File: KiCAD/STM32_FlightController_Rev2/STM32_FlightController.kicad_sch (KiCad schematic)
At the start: 71 parts, among them J1 USB_B_Micro, J10 Serial Debug Pins, J11 GPS_V_{IN}, J12 GPS_TX, J13 GND, J14 GPS_RX, J15 ELRS_V_{IN}, J16 GND, J17 ELRS_TX, J18 ELRS_RX, J2 GND, J3 BAT, J4 CRT, J5 5V, J6 S1, J7 S2, J8 S3, J9 S4, Q1 IRLML6244, Q2 IRLML6244, SW1 PTS815SJM, SW2 SW_SPDT, U1 USBLC6-2SC6, U2 AMS1117-3.3, U3 TLV70018, U4 STM32F405RGTx, U5 BMP390L, U6 ICM-20948, Y1 8MHz

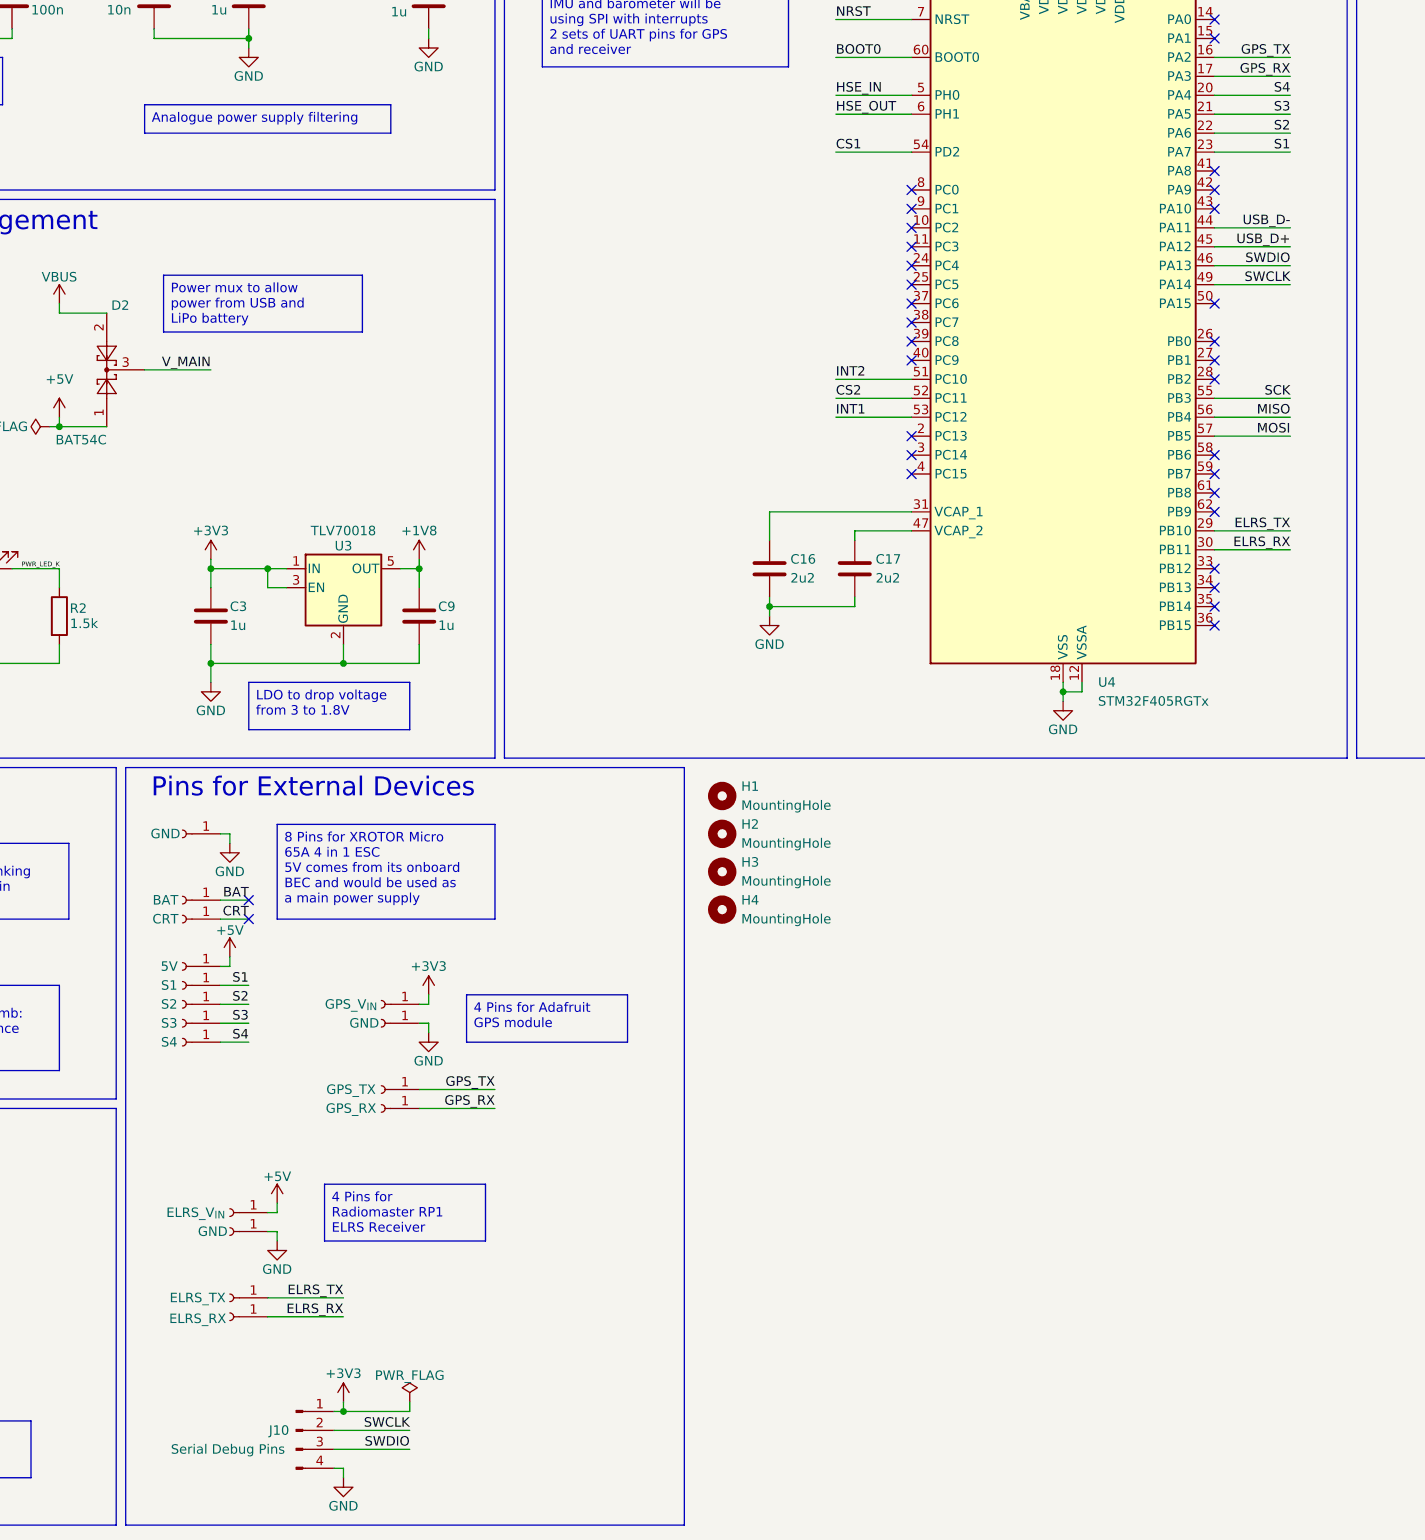
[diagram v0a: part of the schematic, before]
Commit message: added firmware framework, some PCB modifications
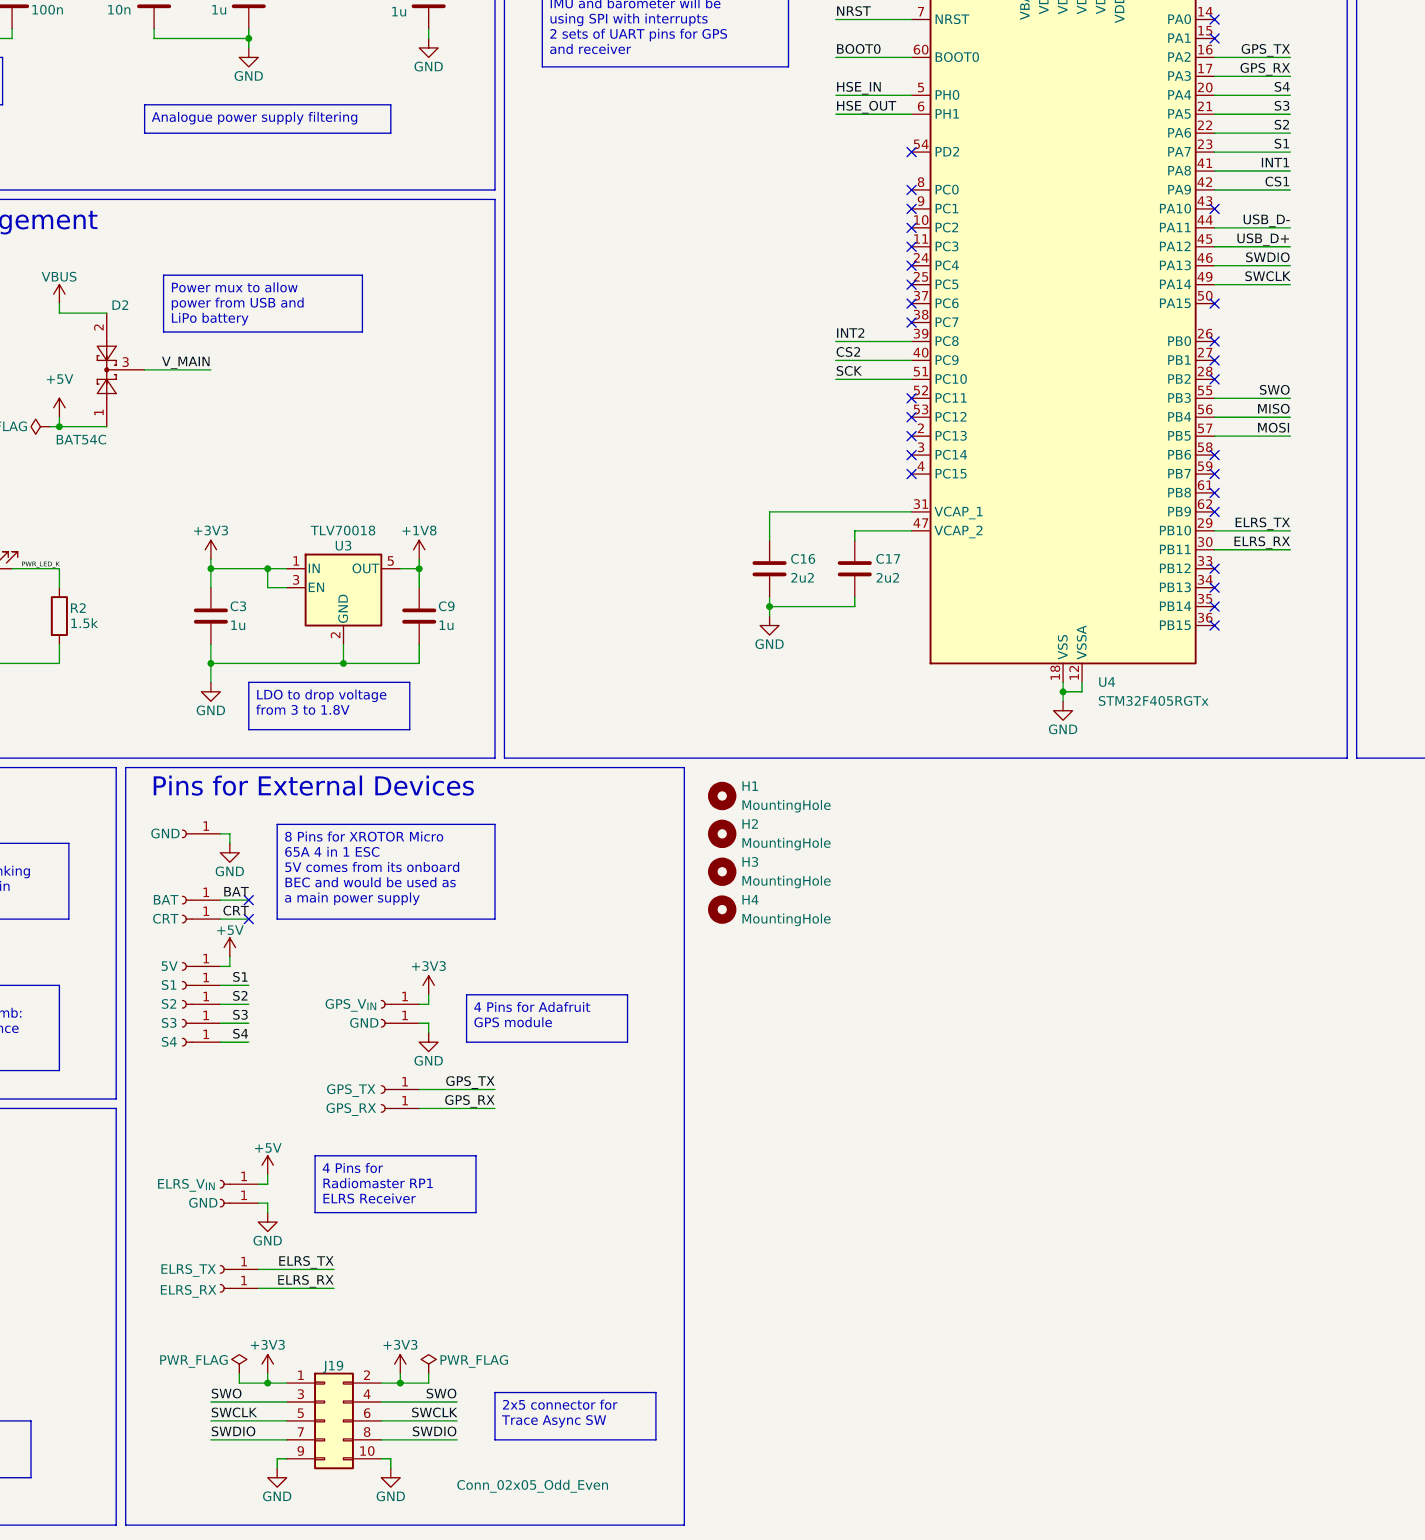
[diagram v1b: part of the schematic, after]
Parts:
- removed J10: Serial Debug Pins, Connector_PinHeader_2.54mm:PinHeader_1x04_P2.54mm_Vertical, symbol Connector:Conn_01x04_Pin
- added J19: Conn_02x05_Odd_Even, Connector_PinHeader_1.27mm:PinHeader_2x05_P1.27mm_Vertical, symbol Connector_Generic:Conn_02x05_Odd_Even
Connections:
- net +3V3: now also J19.1 (Pin_1), J19.2 (Pin_2)
- net CS1: now also U4.42 (PA9); no longer U4.54 (PD2)
- net CS2: now also U4.40 (PC9); no longer U4.52 (PC11)
- net GND: now also J19.10 (Pin_10), J19.9 (Pin_9)
- net INT1: now also U4.41 (PA8); no longer U4.53 (PC12)
- net INT2: now also U4.39 (PC8); no longer U4.51 (PC10)
- net SCK: now also U4.51 (PC10); no longer U4.55 (PB3)
- net SWCLK: now also J19.5 (Pin_5), J19.6 (Pin_6)
- net SWDIO: now also J19.7 (Pin_7), J19.8 (Pin_8)
- new net SWO: J19.3 (Pin_3), J19.4 (Pin_4), U4.55 (PB3)
- no-connect marks 37 -> 36

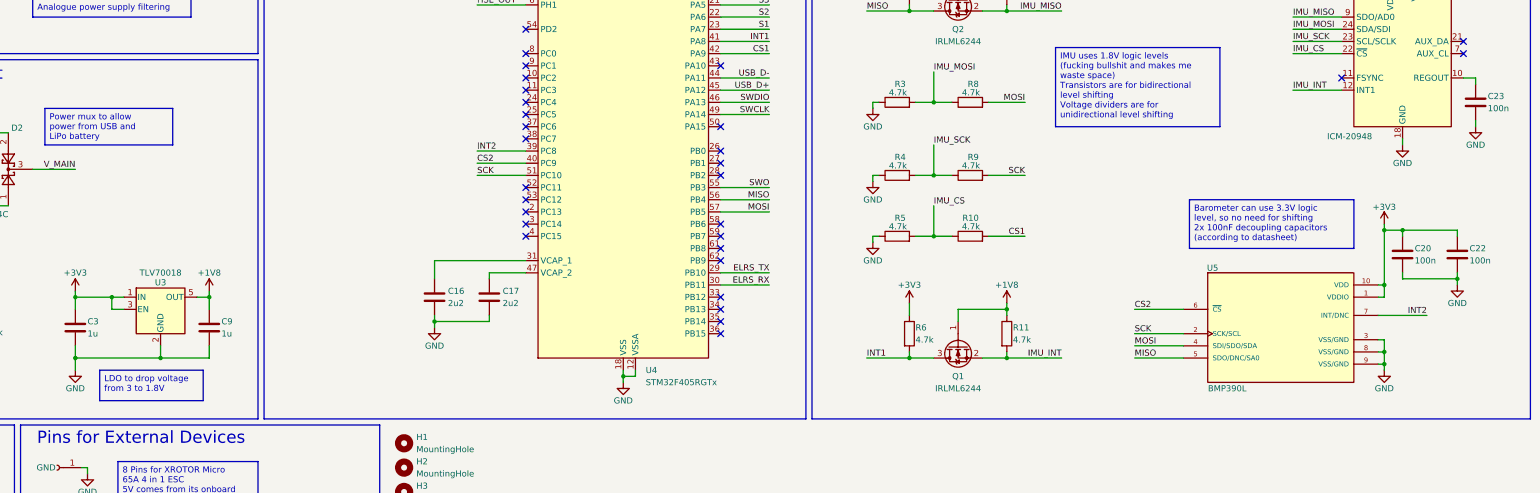
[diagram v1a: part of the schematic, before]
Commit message: corrected BMP390 schematic wiring and layout, among other corrections
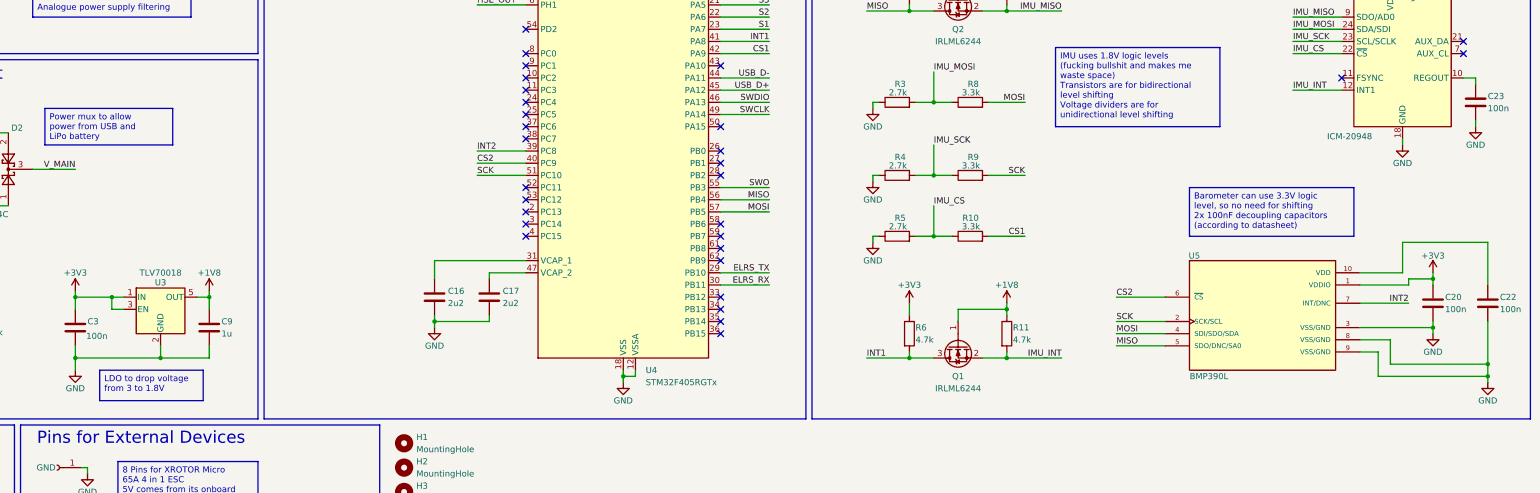
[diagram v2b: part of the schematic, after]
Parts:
- C3: value 1u -> 100n
- R10, R8, R9: value 4.7k -> 3.3k
- R3, R4, R5: value 4.7k -> 2.7k
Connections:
- net +3V3: no longer C22.1, U5.10 (VDD)
- new net: C22.1, U5.10 (VDD)
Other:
- moved on the sheet: C20, C22, U5

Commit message: fixed respective RX and TX wirings
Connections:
- net ELRS_RX: now also U4.29 (PB10); no longer U4.30 (PB11)
- net ELRS_TX: now also U4.30 (PB11); no longer U4.29 (PB10)
- net GPS_RX: now also U4.16 (PA2); no longer U4.17 (PA3)
- net GPS_TX: now also U4.17 (PA3); no longer U4.16 (PA2)
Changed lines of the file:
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@@
 		)
 	)
-	(text_box "IMU uses 1.8V logic levels (fucking bullshit and makes me waste space)\nTransistors are for bidirectional level shifting\nVoltage dividers are for unidirectional level shifting"
+	(text_box "IMU uses 1.8V logic levels (fucking bullshit and makes me waste space)\nTransistors are for unidirectional level shifting up (1.8V -> 3.3V)\nVoltage dividers are for unidirectional level shifting down (3.3 -> 1.8V)"
 		(exclude_from_sim no)
-		(at 306.07 54.61 0)
-		(size 34.29 16.51)
+		(at 303.53 55.88 0)
+		(size 40.64 15.24)
 		(margins 0.9525 0.9525 0.9525 0.9525)
 		(stroke
@@
 		)
 	)
-	(label "GPS_RX"
+	(label "GPS_TX"
 		(at 246.38 40.64 180)
 		(effects
@@
 		)
 	)
-	(label "ELRS_TX"
+	(label "ELRS_RX"
 		(at 246.38 101.6 180)
 		(effects
@@
 		)
 	)
-	(label "GPS_TX"
+	(label "GPS_RX"
 		(at 246.38 38.1 180)
 		(effects
@@
 		)
 	)
-	(label "ELRS_RX"
+	(label "ELRS_TX"
 		(at 246.38 104.14 180)
 		(effects

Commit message: suggested fixes
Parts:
- added D3: PMEG6010CEH, Diode_SMD:D_SOD-123F, symbol Diode:PMEG6010CEH
- R10, R8, R9: value 3.3k -> 2.7k
- R3, R4, R5: value 2.7k -> 3.3k
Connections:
- net +3V3: now also C22.1, U5.10 (VDD)
- no-connect marks 36 -> 38
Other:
- note added: "High Speed External Crystal"
- note removed: "High Speed External Oscillator"
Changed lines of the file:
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@@
 		)
 	)
-	(text "High Speed External Oscillator"
+	(text "High Speed External Crystal"
 		(exclude_from_sim no)
-		(at 43.18 136.144 0)
+		(at 40.64 136.144 0)
 		(effects
 			(font
@@
 	(text "RESET and BOOT Functionality"
 		(exclude_from_sim no)
-		(at 43.18 181.864 0)
+		(at 42.672 181.864 0)
 		(effects
 			(font
@@
 		)
 	)
+	(text_box "*need to change power mux to a component with higher Amp rating"
+		(exclude_from_sim no)
+		(at 91.44 82.55 0)
+		(size 26.67 7.62)
+		(margins 0.9525 0.9525 0.9525 0.9525)
+		(stroke
+			(width 0)
+			(type solid)
+		)
+		(fill
+			(type none)
+		)
+		(effects
+			(font
+				(size 1.27 1.27)
+			)
+			(justify left top)
+		)
+	)
 	(text_box "Barometer can use 3.3V logic level, so no need for shifting\n2x 100nF decoupling capacitors (according to datasheet)"
 		(exclude_from_sim no)
@@
 		)
 	)
+	(text_box "*should change it to dedicated level shifter IC"
+		(exclude_from_sim no)
+		(at 312.42 38.1 0)
+		(size 33.02 6.35)
+		(margins 0.9525 0.9525 0.9525 0.9525)
+		(stroke
+			(width 0)
+			(type solid)
+		)
+		(fill
+			(type none)
+		)
+		(effects
+			(font
+				(size 1.27 1.27)
+			)
+			(justify left top)
+		)
+	)
 	(text_box "LDO to drop voltage from 5 to 3.3V"
 		(exclude_from_sim no)
@@
 	)
 	(junction
+		(at 396.24 95.25)
+		(diameter 0)
+		(color 0 0 0 0)
+	)
+	(junction
 		(at 384.81 113.03)
 		(diameter 0)
@@
 	)
 	(no_connect
+		(at 81.28 100.33)
+	)
+	(no_connect
 		(at 391.16 55.88)
 	)
@@
 	)
 	(no_connect
+		(at 81.28 92.71)
+	)
+	(no_connect
 		(at 195.58 71.12)
 	)
@@
 	(wire
 		(pts
+			(xy 396.24 93.98) (xy 396.24 95.25)
+		)
+		(stroke
+			(width 0)
+			(type default)
+		)
+	)
+	(wire
+		(pts
 			(xy 48.26 224.79) (xy 55.88 224.79)
 		)
@@
 	)
 	(symbol
+		(lib_id "Diode:PMEG6010CEH")
+		(at 81.28 96.52 90)
+		(unit 1)
+		(exclude_from_sim no)
+		(in_bom yes)
+		(on_board yes)
+		(dnp no)
+		(fields_autoplaced yes)
+		(property "Reference" "D3"
+			(at 83.82 95.5674 90)
+			(effects
+				(font
+					(size 1.27 1.27)
+				)
+				(justify right)
+			)
+		)
+		(property "Value" "PMEG6010CEH"
+			(at 83.82 98.1074 90)
+			(effects
+				(font
+					(size 1.27 1.27)
+				)
+				(justify right)
+			)
+		)
+		(property "Footprint" "Diode_SMD:D_SOD-123F"
+			(at 85.725 96.52 0)
+			(effects
+				(font
+					(size 1.27 1.27)
+				)
+				(hide yes)
+			)
+		)
+		(property "Datasheet" "https://assets.nexperia.com/documents/data-sheet/PMEG6010CEH_PMEG6010CEJ.pdf"
+			(at 81.28 96.52 0)
+			(effects
+				(font
+					(size 1.27 1.27)
+				)
+				(hide yes)
+			)
+		)
+		(property "Description" "60V, 1A very low Vf MEGA Schottky barrier rectifier, SOD-123F"
+			(at 81.28 96.52 0)
+			(effects
+				(font
+					(size 1.27 1.27)
+				)
+				(hide yes)
+			)
+		)
+		(pin "2"
+		)
+		(pin "1"
+		)
+		(instances
+			(project ""
+				(path "/a6fc9d05-aa55-4563-bf4c-1c56ae2e96b7"
+					(reference "D3")
+					(unit 1)
+				)
+			)
+		)
+	)
+	(symbol
 		(lib_id "Device:C")
 		(at 29.21 114.3 0)
@@
 			)
 		)
-		(property "Value" "3.3k"
+		(property "Value" "2.7k"
 			(at 290.322 79.248 90)
 			(effects
@@
 			)
 		)
-		(property "Value" "3.3k"
+		(property "Value" "2.7k"
 			(at 290.322 64.008 90)
 			(effects
@@
 			)
 		)
-		(property "Value" "3.3k"
+		(property "Value" "2.7k"
 			(at 290.322 91.948 90)
 			(effects
@@
 			)
 		)
-		(property "Value" "2.7k"
+		(property "Value" "3.3k"
 			(at 275.082 91.948 90)
 			(effects
@@
 	)
 	(symbol
+		(lib_id "power:+3V3")
+		(at 396.24 93.98 0)
+		(unit 1)
+		(exclude_from_sim no)
+		(in_bom yes)
+		(on_board yes)
+		(dnp no)
+		(property "Reference" "#PWR050"
+			(at 396.24 97.79 0)
+			(effects
+				(font
+					(size 1.27 1.27)
+				)
+				(hide yes)
+			)
+		)
+		(property "Value" "+3V3"
+			(at 396.24 90.424 0)
+			(effects
+				(font
+					(size 1.27 1.27)
+				)
+			)
+		)
+		(property "Footprint" ""
+			(at 396.24 93.98 0)
+			(effects
+				(font
+					(size 1.27 1.27)
+				)
+				(hide yes)
+			)
+		)
+		(property "Datasheet" ""
+			(at 396.24 93.98 0)
+			(effects
+				(font
+					(size 1.27 1.27)
+				)
+				(hide yes)
+			)
+		)
+		(property "Description" "Power symbol creates a global label with name \"+3V3\""
+			(at 396.24 93.98 0)
+			(effects
+				(font
+					(size 1.27 1.27)
+				)
+				(hide yes)
+			)
+		)
+		(pin "1"
+		)
+		(instances
+			(project "STM32_FlightController"
+				(path "/a6fc9d05-aa55-4563-bf4c-1c56ae2e96b7"
+					(reference "#PWR050")
+					(unit 1)
+				)
+			)
+		)
+	)
+	(symbol
 		(lib_id "Device:Crystal_GND24")
 		(at 29.21 156.21 0)
@@
 			)
 		)
-		(property "Value" "2.7k"
+		(property "Value" "3.3k"
 			(at 275.082 64.008 90)
 			(effects
@@
 			)
 		)
-		(property "Value" "2.7k"
+		(property "Value" "3.3k"
 			(at 275.082 79.248 90)
 			(effects

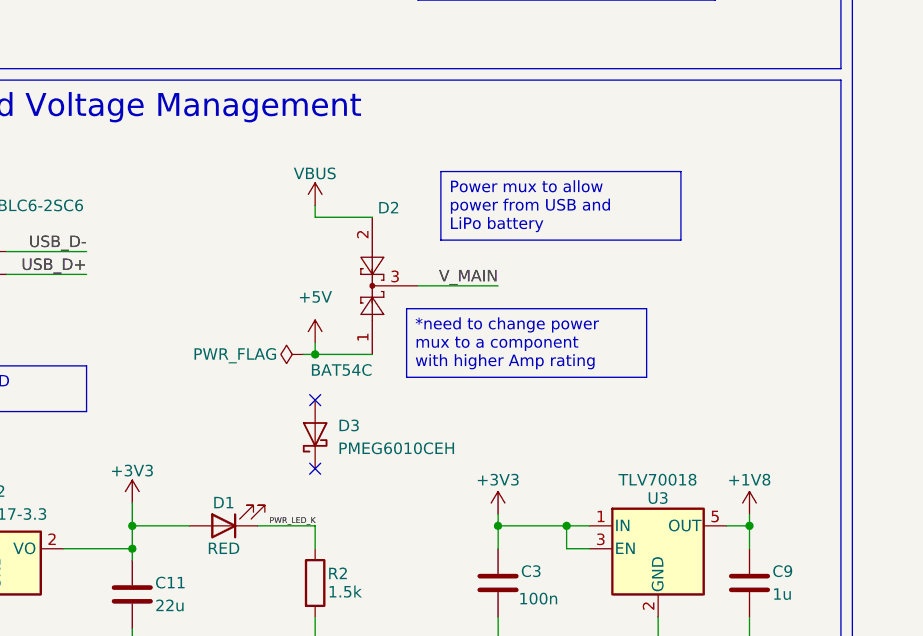
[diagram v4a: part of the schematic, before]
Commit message: re-speccing the power mux to PMEG2005CT,215 rated for 500 mA
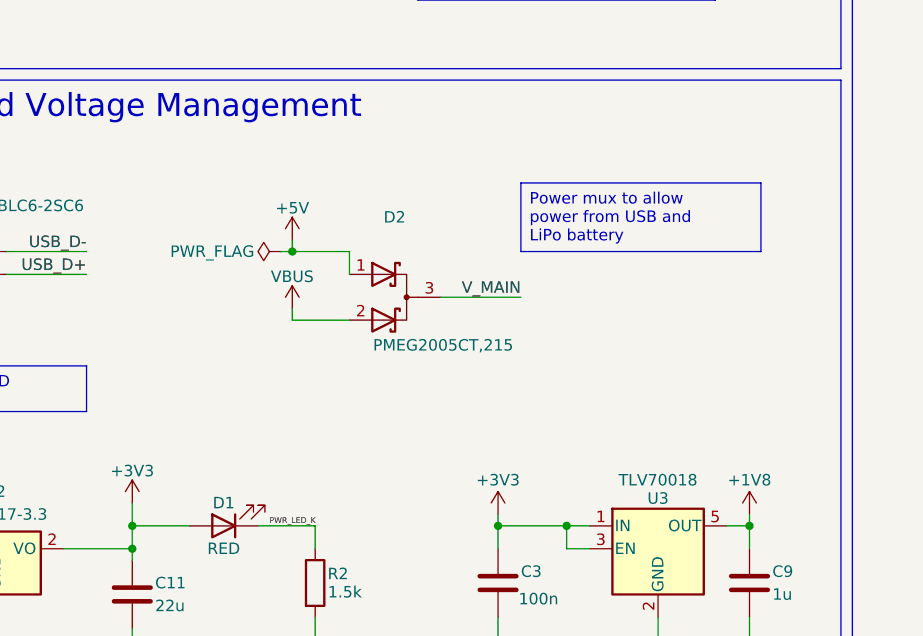
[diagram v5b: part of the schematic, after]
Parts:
- removed D2: BAT54C, Package_TO_SOT_SMD:SOT-23, symbol Diode:BAT54C
- removed D3: PMEG6010CEH, Diode_SMD:D_SOD-123F, symbol Diode:PMEG6010CEH
- added D2: PMEG2005CT,215, Package_TO_SOT_SMD:SOT-23, symbol Device:D_Schottky_Dual_CommonCathode_AAK_Parallel
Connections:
- net +5V: now also D2.1 (A)
- net VBUS: now also D2.2 (A)
- net V_MAIN: now also D2.3 (K)
- no-connect marks 38 -> 36
